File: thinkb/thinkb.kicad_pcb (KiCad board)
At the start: 2 copper layers, 298.9 x 142.9 mm, 149 parts, among them P1 battery+, P2 battery-, SW1 SW_Push, SW11 SW_Push, SW12 SW_Push, SW13 SW_Push, SW14 SW_Push, SW15 SW_Push, SW16 SW_Push, SW17 SW_Push, SW18 SW_Push, SW19 SW_Push, SW2 SW_Push, SW20 SW_Push, SW21 SW_Push, SW22 SW_Push, SW23 SW_Push, SW24 SW_Push, SW25 SW_Push, SW26 SW_Push, SW27 SW_Push, SW28 SW_Push, SW29 SW_Push, SW3 SW_Push, SW30 SW_Push, SW31 SW_Push, SW32 SW_Push, SW33 SW_Push, SW34 SW_Push, SW35 SW_Push, SW36 SW_Push, SW37 SW_Push, SW38 SW_Push, SW39 SW_Push, SW4 SW_Push, SW40 SW_Push, SW41 SW_Push, SW42 SW_Push, SW43 SW_Push, SW44 SW_Push, SW45 SW_Push, SW46 SW_Push, SW47 SW_Push, SW48 SW_Push, SW49 SW_Push, SW5 SW_Push, SW50 SW_Push, SW51 SW_Push, SW52 SW_Push, SW53 SW_Push, SW54 SW_Push, SW55 SW_Push, SW56 SW_Push, SW57 SW_Push, SW58 SW_Push, SW59 SW_Push, SW6 SW_Push, SW60 SW_Push, SW61 SW_Push, SW62 Reset, SW63 Power, SW7 SW_Push, SW8 SW_Push, SW9 SW_Push

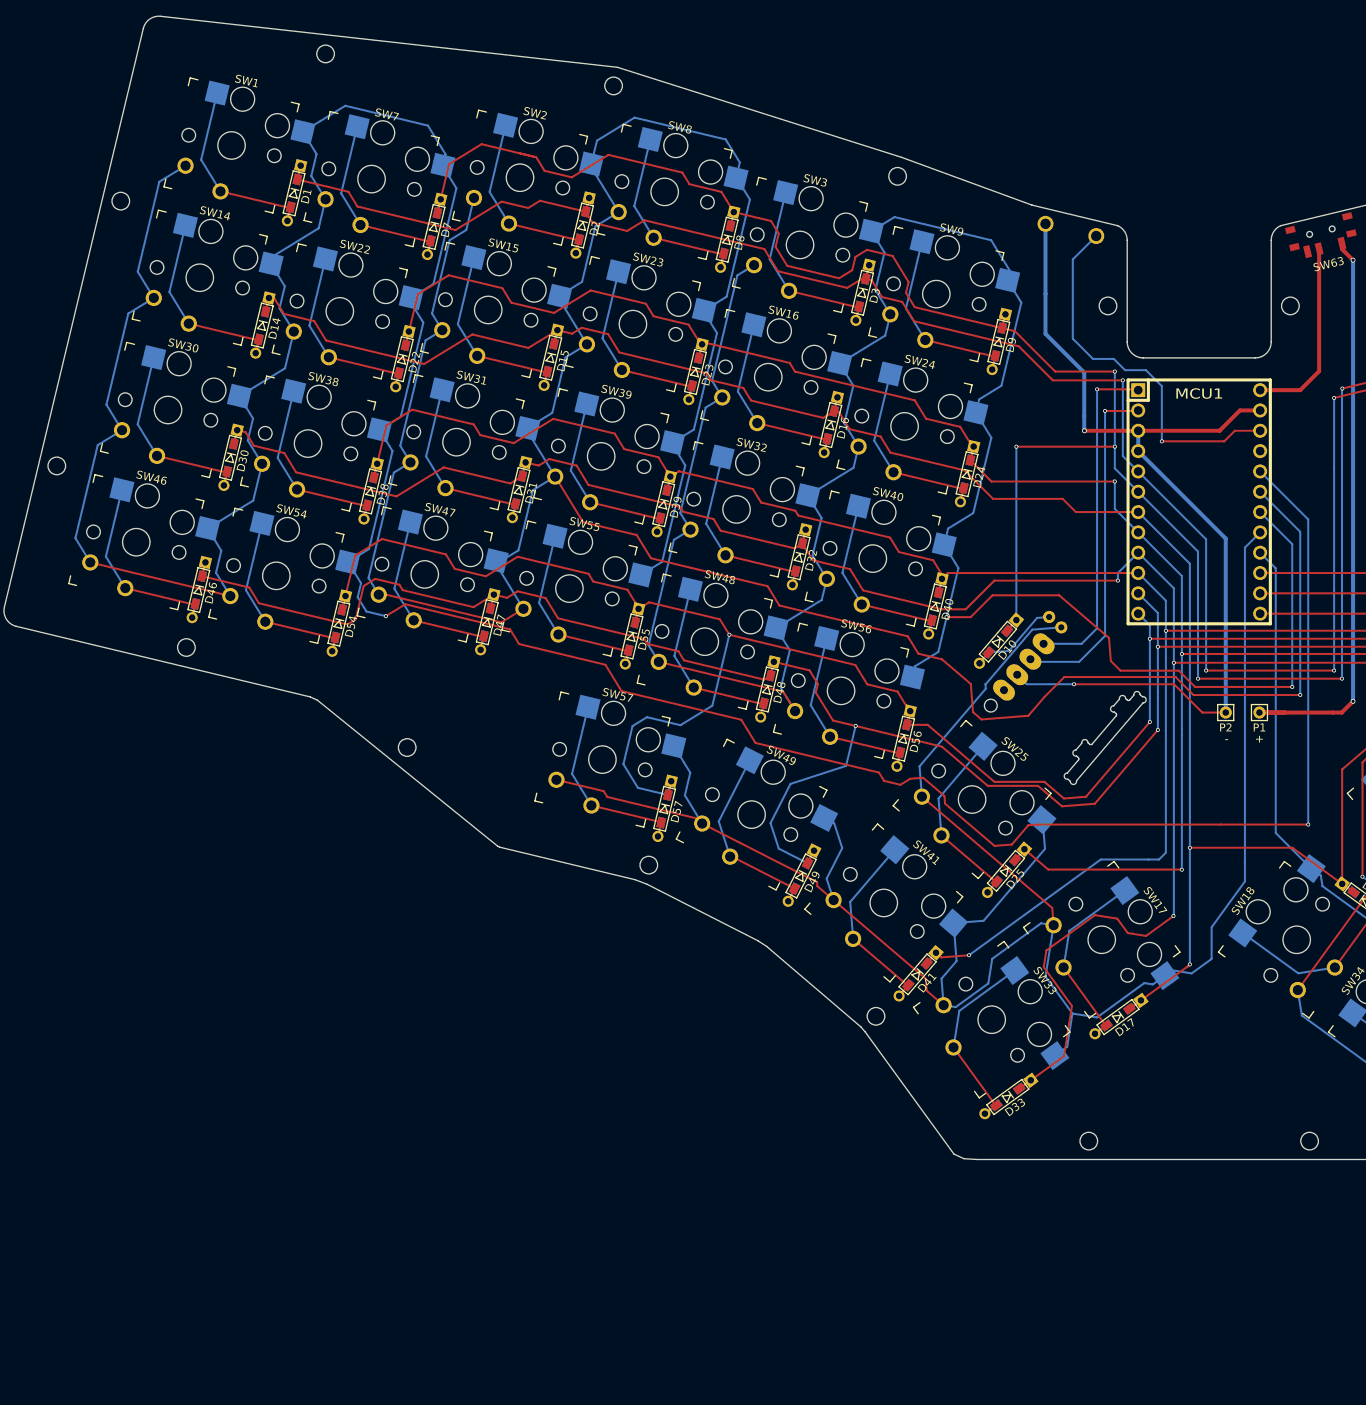
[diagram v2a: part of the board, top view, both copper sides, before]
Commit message: Working on mounting holes
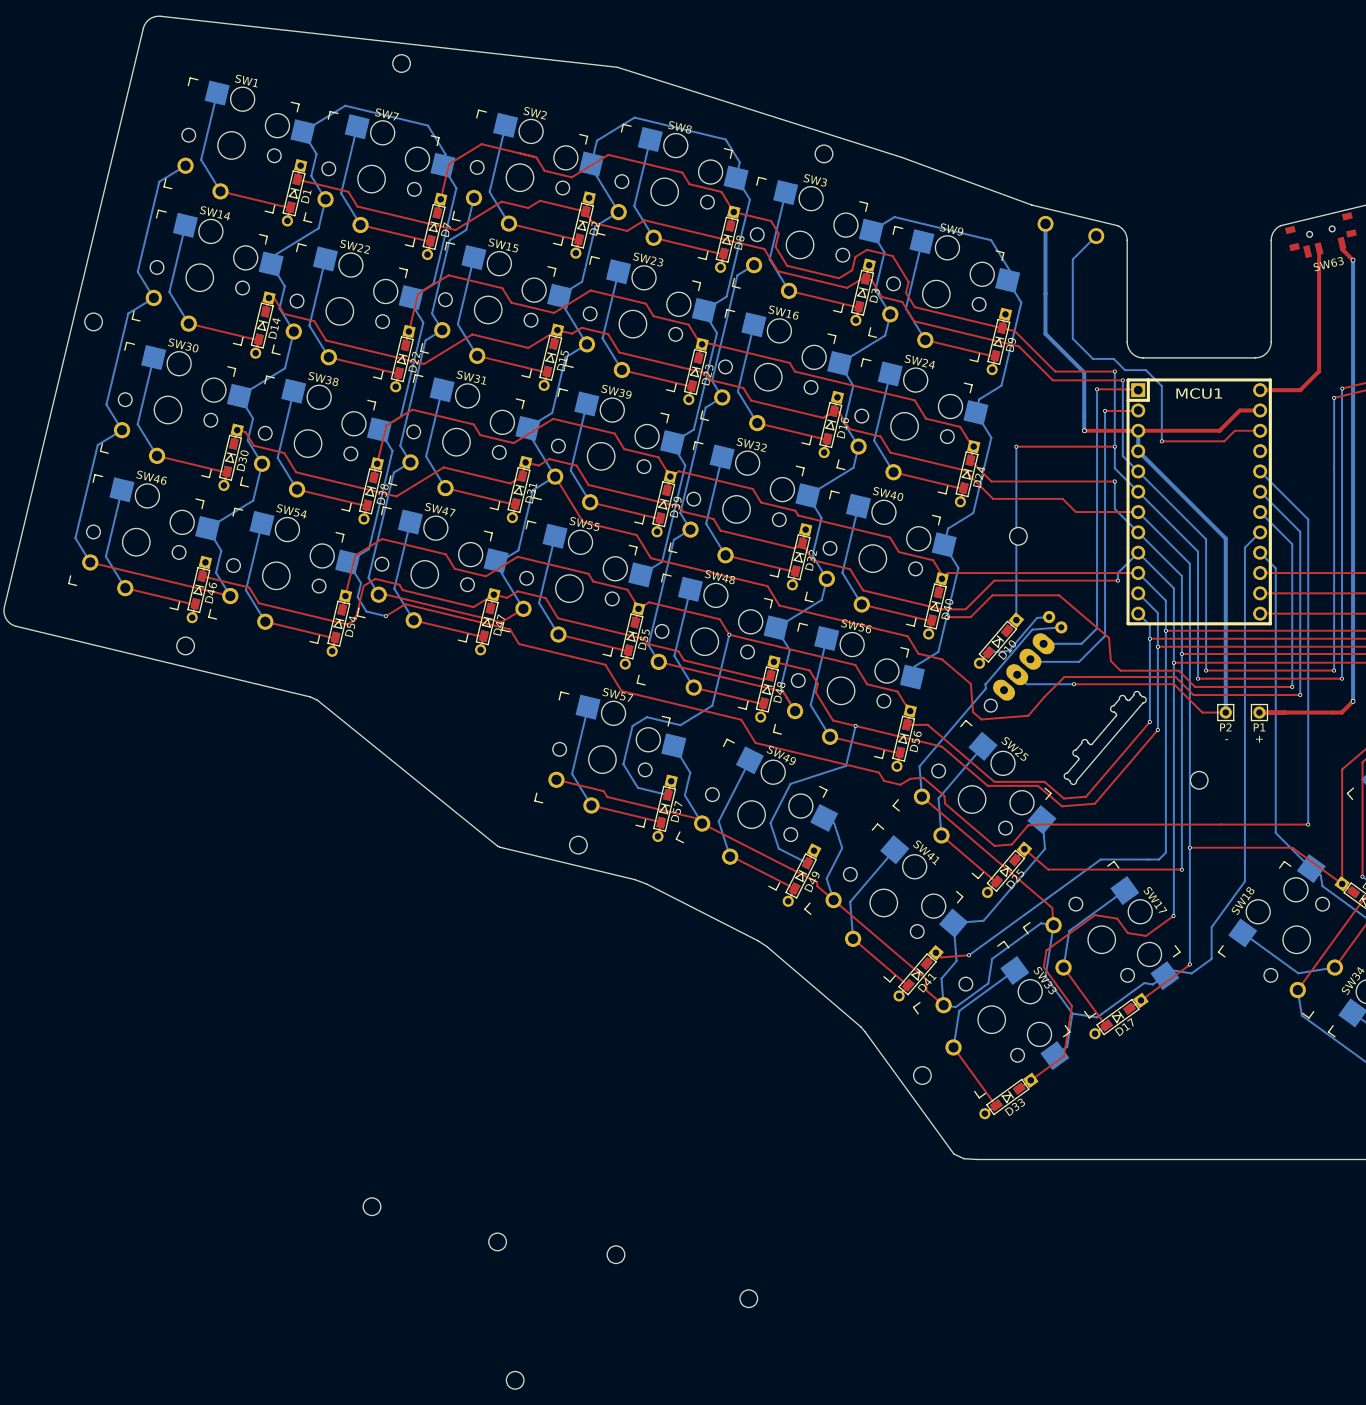
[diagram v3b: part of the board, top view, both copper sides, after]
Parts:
- moved H8 162.3 mm to (-85.5, 109.8)
- moved H5 111.6 mm to (-87.7, 92.5)
- moved H23 72.8 mm to (-56.3, 99.6)
- moved H10 60.4 mm to (0.00, 34.8)
- moved H9 57.6 mm to (-103.4, 88.1)
- moved H17 44.1 mm to (-72.9, 94.1)
- moved H6 30.9 mm to (-22.6, 4.30)
- moved H1 22.4 mm to (-34.6, 71.7)
- moved H16 15.5 mm to (-138.2, -22.5)
- moved H20 9.62 mm to (-46.9, -43.5)
- moved H12 9.58 mm to (-99.7, -54.8)
- moved H13 9.15 mm to (-77.6, 42.9)
- moved H3 0.22 mm to (-126.7, 18.0)

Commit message: Mountin holes
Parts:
- moved H8 162.2 mm to (-73.2, -51.9)
- moved H23 142.8 mm to (11.5, -26.1)
- moved H17 135.0 mm to (-11.5, -26.1)
- moved H7 110.4 mm to (0.00, 79.6)
- moved H21 75.7 mm to (22.6, 4.30)
- moved H19 63.2 mm to (73.2, -51.9)
- moved H15 17.0 mm to (138.6, -21.0)
- moved H18 9.62 mm to (46.9, -43.5)
- moved H22 9.58 mm to (99.7, -54.8)
- moved H2 9.40 mm to (34.6, 71.7)
- moved H4 9.15 mm to (77.6, 42.9)
- moved H10 2.90 mm to (0.00, 37.7)
- moved H16 1.55 mm to (-138.6, -21.0)
- moved H11 0.22 mm to (126.7, 18.0)
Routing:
- net row2: track 416.0 -> 419.7 mm
- net row3: track 388.3 -> 391.3 mm
- net row1: track 379.1 -> 381.9 mm
- net row5: track 391.0 -> 389.3 mm
- net col0: track 410.4 -> 411.2 mm
- net row4: track 453.3 -> 454.0 mm
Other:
- outline, holes or cut-outs redrawn

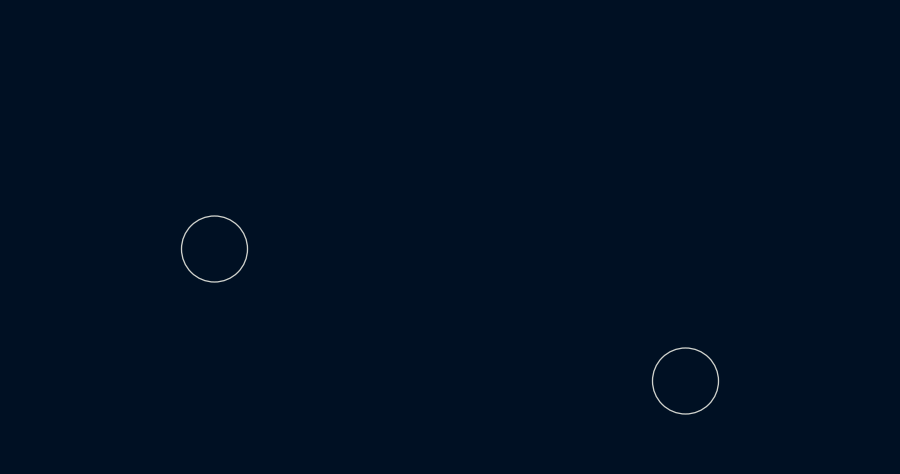
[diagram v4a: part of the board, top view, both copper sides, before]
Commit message: Removed extra holes
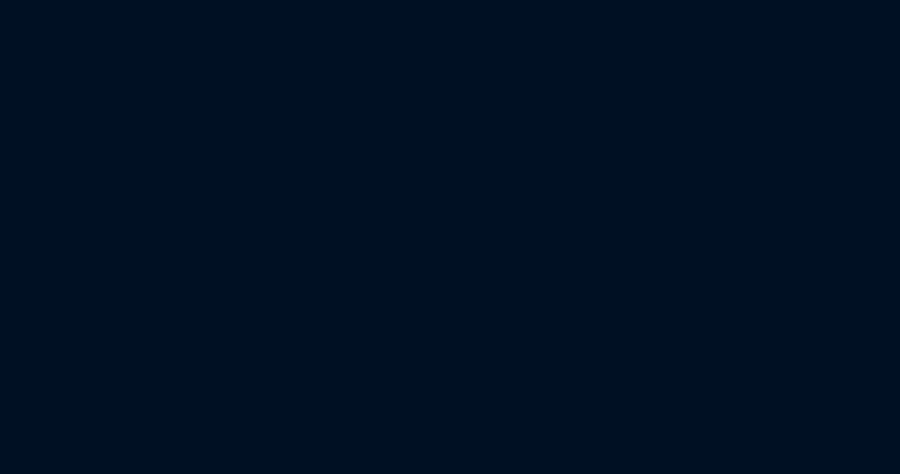
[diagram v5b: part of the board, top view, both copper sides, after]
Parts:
- removed H5, H9: MountingHole, MountingHole:MountingHole_2.2mm_M2
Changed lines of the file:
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@@
     (tracks 1807)
     (zones 0)
-    (modules 149)
+    (modules 147)
     (nets 84)
   )
@@
     (add_net "Net-(D8-Pad2)")
     (add_net "Net-(D9-Pad2)")
+    (add_net "Net-(ENC2-PadNC)")
+    (add_net "Net-(MCU1-Pad21)")
     (add_net "Net-(MCU1-Pad22)")
     (add_net "Net-(MCU1-Pad24)")
     (add_net "Net-(P1-Pad1)")
+    (add_net "Net-(SW63-Pad3)")
     (add_net col0)
     (add_net col1)
@@
   )
   (module MountingHole:MountingHole_2.2mm_M2 (layer F.Cu)
-    (at -87.7 92.5)
-    (descr "Mounting Hole 2.2mm, no annular, M2")
-    (tags "mounting hole 2.2mm no annular m2")
-    (attr virtual)
-    (fp_text reference H5 (at 0 -3.2) (layer F.SilkS) hide
-      (effects (font (size 1 1) (thickness 0.15)))
-    )
-    (fp_text value MountingHole (at 0 3.2) (layer F.Fab) hide
-      (effects (font (size 1 1) (thickness 0.15)))
-    )
-    (fp_circle (center 0 0) (end 2.45 0) (layer F.CrtYd) (width 0.05))
-    (fp_circle (center 0 0) (end 2.2 0) (layer Cmts.User) (width 0.15))
-    (fp_text user %R (at 0.3 0) (layer F.Fab) hide
-      (effects (font (size 1 1) (thickness 0.15)))
-    )
-    (pad 1 np_thru_hole circle (at 0 0) (size 2.2 2.2) (drill 2.2) (layers *.Cu *.Mask))
-  )
-  (module MountingHole:MountingHole_2.2mm_M2 (layer F.Cu)
     (at 0 79.6)
     (descr "Mounting Hole 2.2mm, no annular, M2")
@@
   )
   (module MountingHole:MountingHole_2.2mm_M2 (layer F.Cu)
-    (at -103.4 88.1)
-    (descr "Mounting Hole 2.2mm, no annular, M2")
-    (tags "mounting hole 2.2mm no annular m2")
-    (attr virtual)
-    (fp_text reference H9 (at 0 -3.2) (layer F.SilkS) hide
-      (effects (font (size 1 1) (thickness 0.15)))
-    )
-    (fp_text value MountingHole (at 0 3.2) (layer F.Fab) hide
-      (effects (font (size 1 1) (thickness 0.15)))
-    )
-    (fp_circle (center 0 0) (end 2.45 0) (layer F.CrtYd) (width 0.05))
-    (fp_circle (center 0 0) (end 2.2 0) (layer Cmts.User) (width 0.15))
-    (fp_text user %R (at 0.3 0) (layer F.Fab) hide
-      (effects (font (size 1 1) (thickness 0.15)))
-    )
-    (pad 1 np_thru_hole circle (at 0 0) (size 2.2 2.2) (drill 2.2) (layers *.Cu *.Mask))
-  )
-  (module MountingHole:MountingHole_2.2mm_M2 (layer F.Cu)

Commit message: Introduced another switch spacing 19x18mm
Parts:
- moved D10 21.9 mm to (-11.7, 34.7)
- moved H13 8.48 mm to (-83.7, 48.8)
- moved D46 7.36 mm to (-132.2, 12.7)
- moved H3 7.36 mm to (-133.9, 19.7)
- moved SW46 7.36 mm to (-140.0, 6.70)
- moved SW53 7.35 mm to (140.0, 6.70)
- moved H11 7.35 mm to (133.9, 19.7)
- moved D53 7.35 mm to (149.7, 8.46)
- moved H15 7.35 mm to (145.8, -19.3)
- moved SW30 6.97 mm to (-135.8, -10.8)
- moved D30 6.97 mm to (-128.0, -4.83)
- moved H16 6.97 mm to (-145.5, -20.3)
- moved D37 6.96 mm to (145.5, -9.04)
- moved SW37 6.96 mm to (135.8, -10.8)
- moved D14 6.71 mm to (-123.8, -22.3)
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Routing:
- net row4: track 454.0 -> 24.6 mm, vias 7 -> 2
- net row2: track 419.7 -> 28.4 mm, vias 4 -> 1
- net row5: track 389.3 -> 14.9 mm, vias 5 -> 0
- net col0: track 411.2 -> 42.1 mm, vias 2 -> 0
- net row6: track 392.6 -> 28.8 mm, vias 4 -> 1
- net row3: track 391.3 -> 33.0 mm, vias 6 -> 2
- net row7: track 364.9 -> 21.9 mm, vias 3 -> 0
- net row0: track 354.7 -> 18.3 mm, vias 4 -> 0
- net row1: track 381.9 -> 52.5 mm, vias 6 -> 1
- net col1: track 363.6 -> 41.7 mm, vias 1 -> 0
- net col6: track 300.1 -> 0.96 mm
- net col7: track 341.6 -> 49.6 mm
- net col3: track 278.0 -> 27.4 mm
- net col2: track 300.8 -> 50.5 mm, vias 2 -> 0
- net col5: track 255.5 -> 23.1 mm
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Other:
- board size 298.9 x 142.9 mm -> 313.2 x 149.2 mm

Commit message: New layout
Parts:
- moved H13 7.68 mm to (-81.7, 41.4)
- moved D7 7.14 mm to (-103.8, -42.0), turned to 259.5 degrees
- moved SW7 6.88 mm to (-111.9, -47.6), turned to 349.5 degrees
- moved SW13 6.88 mm to (111.9, -47.6), turned to 10.5 degrees
- moved D22 6.66 mm to (-107.1, -24.3), turned to 259.5 degrees
- moved D13 6.38 mm to (121.5, -45.3), turned to 280.5 degrees
- moved SW22 6.35 mm to (-115.2, -29.9), turned to 349.5 degrees
- moved SW29 6.35 mm to (115.2, -29.9), turned to 10.5 degrees
- moved D1 6.34 mm to (-122.5, -45.5), turned to 259.5 degrees
- moved ENC2 6.32 mm to (-18.5, 21.9)
- moved D38 6.29 mm to (-110.3, -6.63), turned to 259.5 degrees
- moved SW1 6.12 mm to (-130.6, -51.1), turned to 349.5 degrees
- moved SW6 6.12 mm to (130.6, -51.1), turned to 10.5 degrees
- moved D54 6.04 mm to (-113.6, 11.1), turned to 259.5 degrees
- moved SW38 5.92 mm to (-118.5, -12.2), turned to 349.5 degrees
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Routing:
- net GND: track 37.2 -> 0.00 mm
- net row4: track 24.6 -> 14.2 mm, vias 2 -> 0
- net row3: track 33.0 -> 24.5 mm, vias 2 -> 0
- net row2: track 28.4 -> 22.1 mm
- net Net-(D5-Pad2): track 25.8 -> 22.3 mm
- net Net-(D20-Pad2): track 25.8 -> 22.3 mm
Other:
- board size 313.2 x 149.2 mm -> 313.4 x 149.2 mm
